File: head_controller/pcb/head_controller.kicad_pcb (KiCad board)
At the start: 2 copper layers, 85.6 x 132.2 mm, 79 parts, among them P1 HEADER_02X08_SMD, P2 HEADER_02X05_SMD, U1 HALL_DRV5053, U10 MAX4215, U11 HALL_DRV5053, U12 MAX4215, U13 HALL_DRV5053, U14 MAX4215, U2 MAX4215, U3 HALL_DRV5053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

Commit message: Laid down some tracks.
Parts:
- turned C1 to 180 degrees
- turned C13 to 180 degrees
- turned C16 to 180 degrees
- turned C19 to 180 degrees
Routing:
- net +5V: track 0.00 -> 36.7 mm, vias 0 -> 7
- net GND: track 0.00 -> 23.6 mm, vias 0 -> 7
- net VAA: track 0.00 -> 17.8 mm

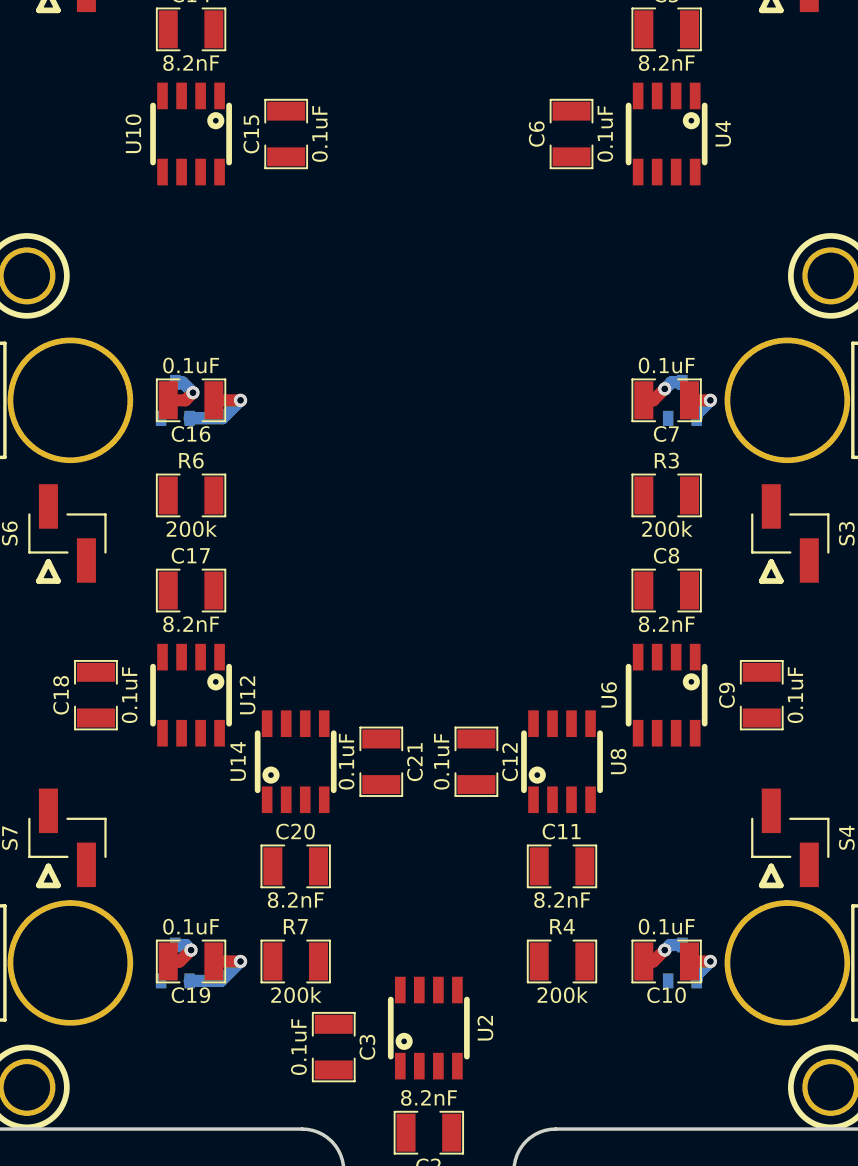
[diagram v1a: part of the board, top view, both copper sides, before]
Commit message: Laid down more tracks manually.
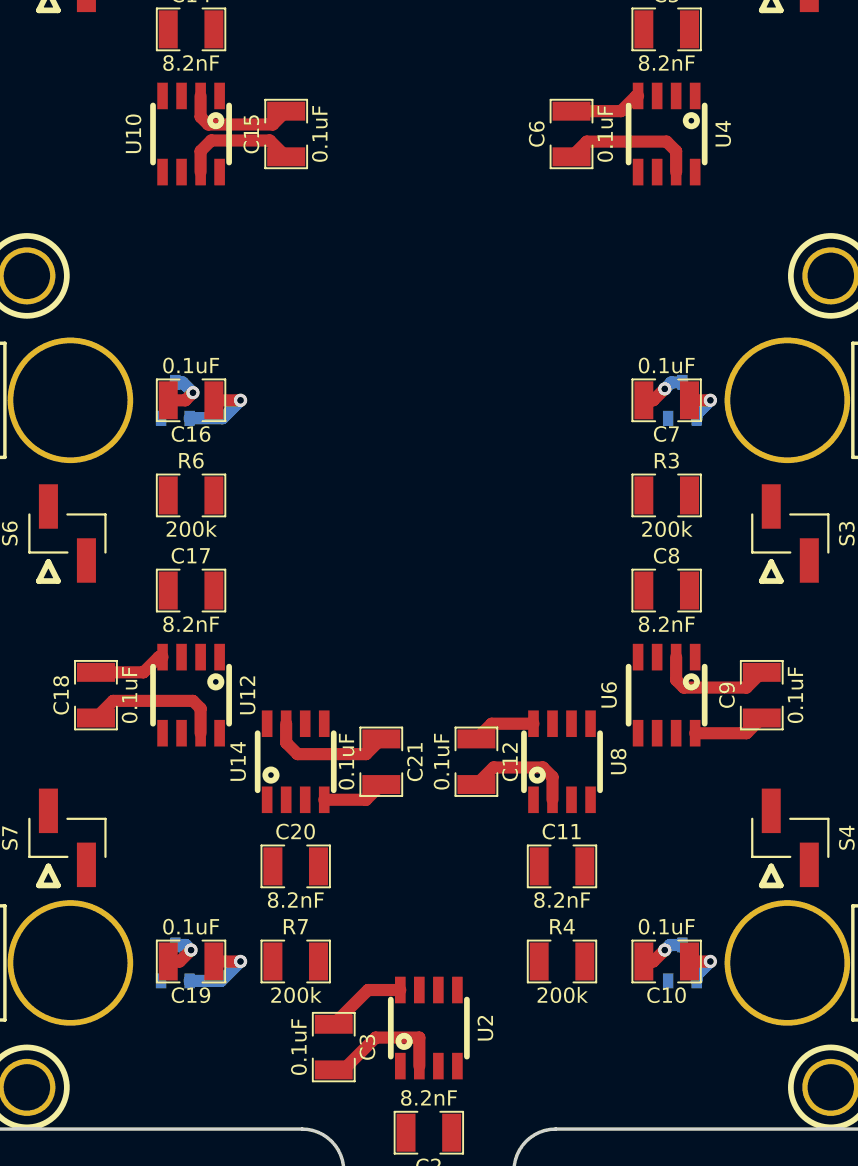
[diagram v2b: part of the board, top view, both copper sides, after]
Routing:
- net +5V: track 36.7 -> 85.8 mm
- net GND: track 23.6 -> 69.0 mm
